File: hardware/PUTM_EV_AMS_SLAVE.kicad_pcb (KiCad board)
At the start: 4 copper layers, 167.4 x 75.2 mm, 119 parts, among them IC2 BQ79616PAPR, J1 M80-5020442, J2 M80-5020442, J6 522071060, J7 522071060, J8 522071060, Q1 2N7002, Q2 100V/2W, T1 SM91502ALE, T2 SM91502ALE

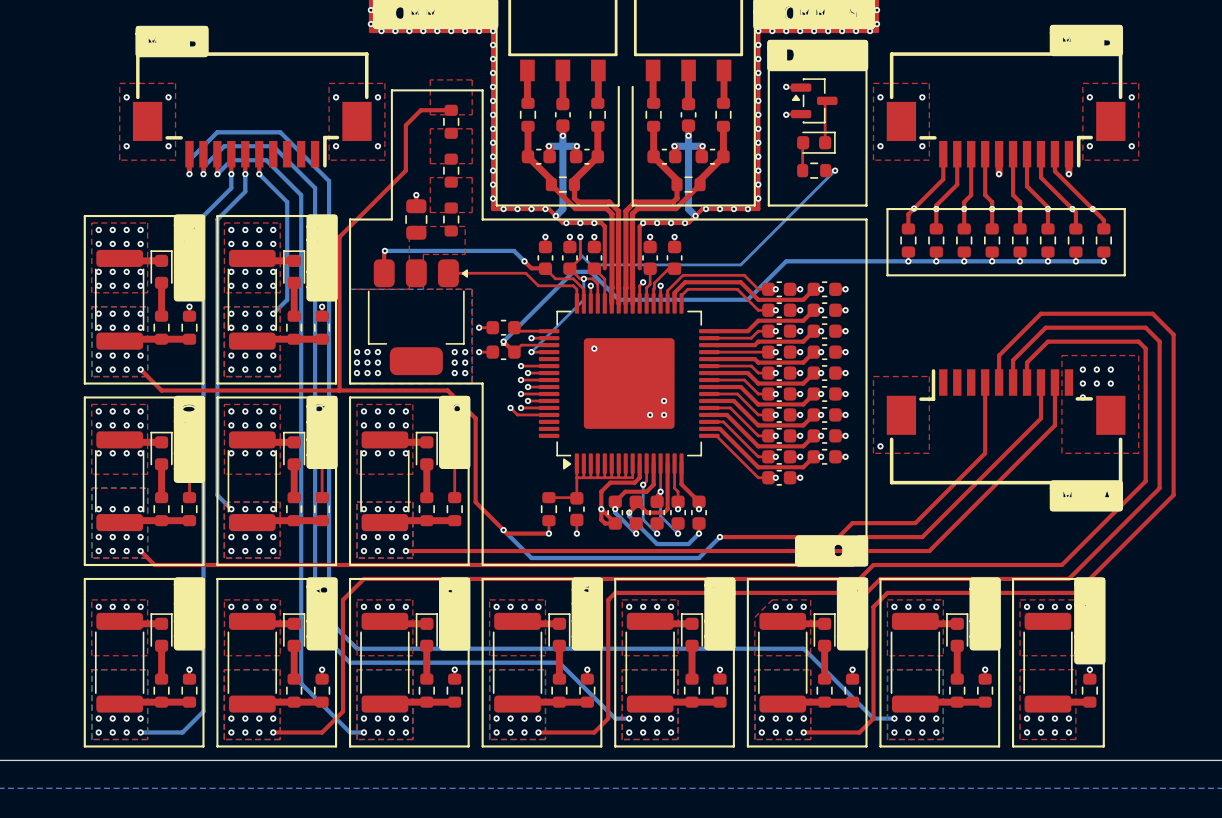
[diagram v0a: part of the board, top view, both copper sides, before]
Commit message: slight fixes
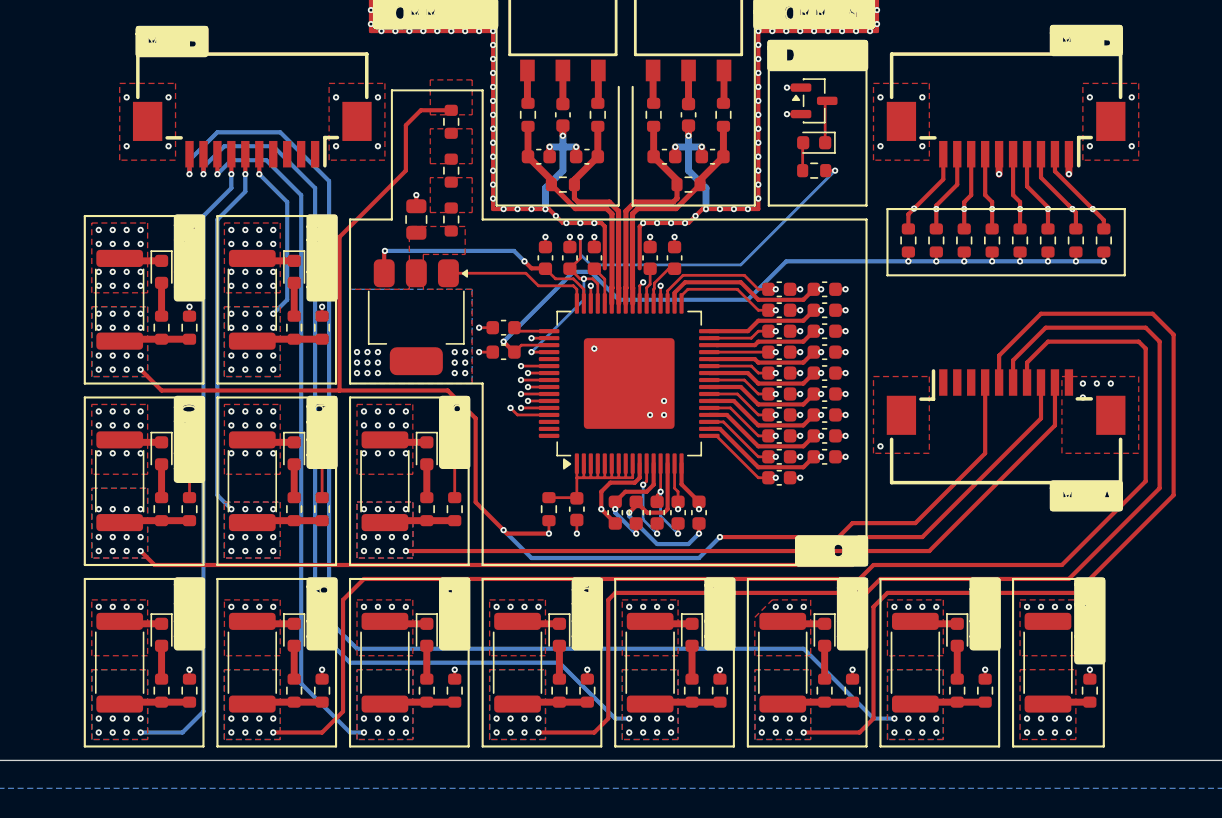
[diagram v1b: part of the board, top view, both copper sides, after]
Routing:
- net /BQ79616/CB12: track 57.0 -> 55.2 mm
- net GND: track 143.3 -> 142.4 mm, vias 153 -> 150
